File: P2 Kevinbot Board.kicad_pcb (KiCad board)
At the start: 2 copper layers, 196.5 x 95.4 mm, 56 parts, among them J11 Screw_Terminal_01x02, J13 Screw_Terminal_01x02, J14 Screw_Terminal_01x02, J17 Conn_01x02, J2 Conn_02x06_Odd_Even, J20 Conn_02x06_Odd_Even, J23 Conn_02x06_Odd_Even, J24 Conn_01x04, J25 Conn_01x04, J26 Conn_01x04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

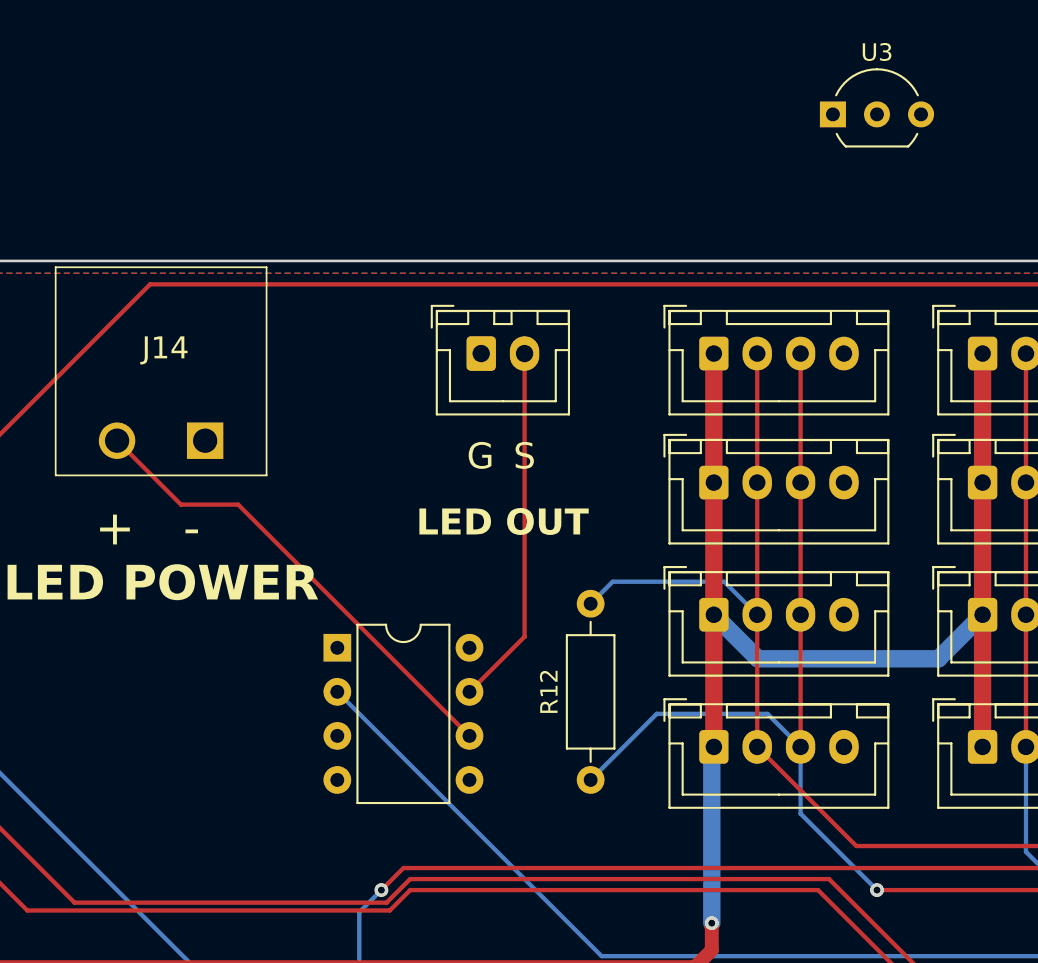
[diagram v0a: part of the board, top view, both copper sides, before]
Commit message: Add DS18B20
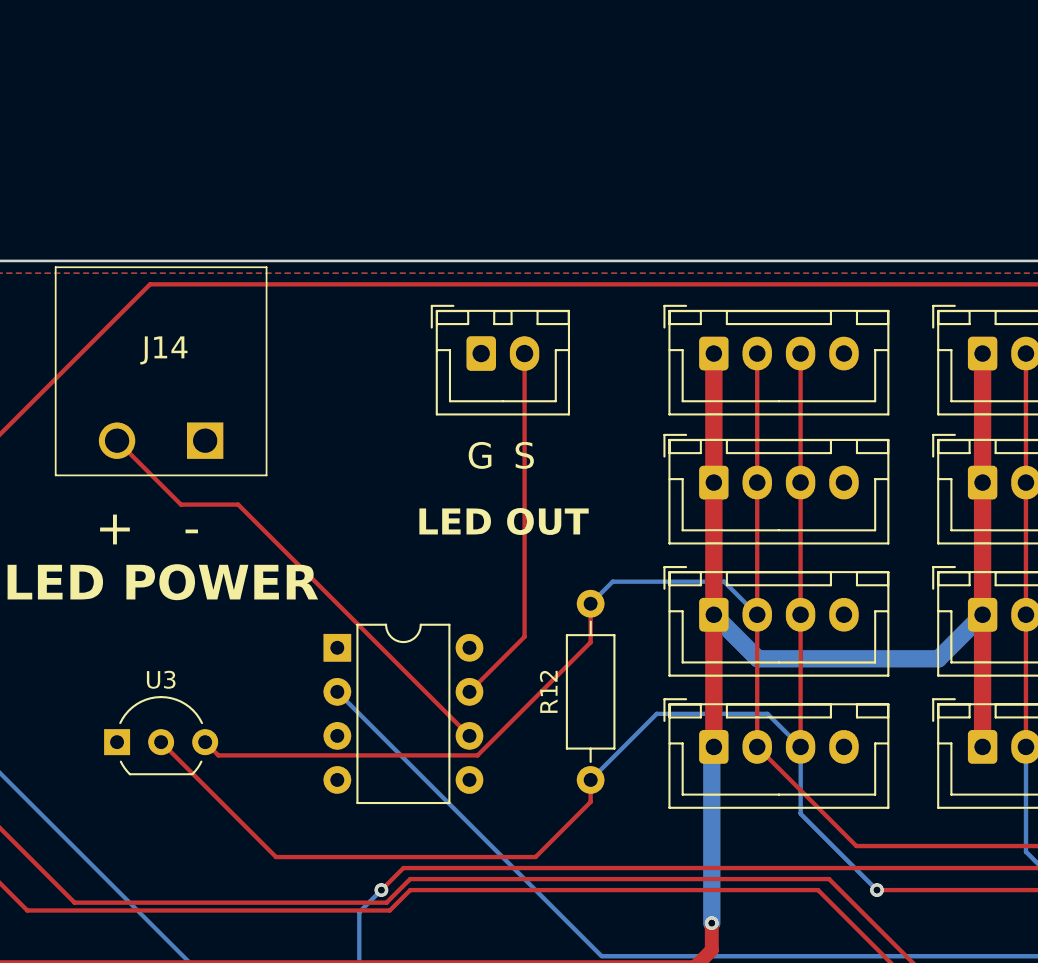
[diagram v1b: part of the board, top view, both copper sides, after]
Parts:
- moved U3 54.9 mm to (103.6, 82.9)
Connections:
- U3 pad 3: P2_V24 -> P2_V32
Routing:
- net P2_P39: track 91.2 -> 121.2 mm
- net P2_V32: track 97.4 -> 124.9 mm
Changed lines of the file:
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@@
   )
   (footprint "Package_TO_SOT_THT:TO-92_Inline_Wide" (layer "F.Cu")
-    (at 144.919 46.72)
+    (at 103.644 82.915)
     (descr "TO-92 leads in-line, wide, drill 0.75mm (see NXP sot054_po.pdf)")
     (tags "to-92 sc-43 sc-43a sot54 PA33 transistor")
@@
       (net 44 "P2_P39") (pinfunction "DQ") (pintype "bidirectional"))
     (pad "3" thru_hole circle (at 5.08 0) (size 1.5 1.5) (drill 0.8) (layers "*.Cu" "*.Mask")
-      (net 66 "P2_V24") (pinfunction "VDD") (pintype "power_in"))
+      (net 43 "P2_V32") (pinfunction "VDD") (pintype "power_in"))
     (model "${KICAD6_3DMODEL_DIR}/Package_TO_SOT_THT.3dshapes/TO-92_Inline_Wide.wrl"
       (offset (xyz 0 0 0))
@@
   (segment (start 189.789 100.216726) (end 189.305726 100.7) (width 0.25) (layer "F.Cu") (net 43))
   (segment (start 182.160726 88.905) (end 189.789 96.533274) (width 0.25) (layer "F.Cu") (net 43))
+  (segment (start 108.724 82.915) (end 109.489 83.68) (width 0.25) (layer "F.Cu") (net 43))
   (segment (start 146.269 88.905) (end 182.160726 88.905) (width 0.25) (layer "F.Cu") (net 43))
   (segment (start 140.554 83.19) (end 146.269 88.905) (width 0.25) (layer "F.Cu") (net 43))
   (segment (start 140.554 83.19) (end 140.554 60.51) (width 0.25) (layer "F.Cu") (net 43))
   (segment (start 189.305726 100.7) (end 187.352274 100.7) (width 0.25) (layer "F.Cu") (net 43))
+  (segment (start 109.489 83.68) (end 124.429991 83.68) (width 0.25) (layer "F.Cu") (net 43))
+  (segment (start 124.429991 83.68) (end 130.949 77.160991) (width 0.25) (layer "F.Cu") (net 43))
   (segment (start 187.352274 100.7) (end 186.424 99.771726) (width 0.25) (layer "F.Cu") (net 43))
+  (segment (start 130.949 77.160991) (end 130.949 74.935) (width 0.25) (layer "F.Cu") (net 43))
   (segment (start 186.424 99.771726) (end 186.424 98.375) (width 0.25) (layer "F.Cu") (net 43))
   (segment (start 189.789 96.533274) (end 189.789 100.216726) (width 0.25) (layer "F.Cu") (net 43))
@@
   (segment (start 187.694 98.375) (end 187.694 96.978274) (width 0.25) (layer "F.Cu") (net 44))
   (segment (start 182.160726 91.445) (end 147.459 91.445) (width 0.25) (layer "F.Cu") (net 44))
+  (segment (start 112.809 89.54) (end 127.774 89.54) (width 0.25) (layer "F.Cu") (net 44))
   (segment (start 143.054 60.51) (end 143.054 83.19) (width 0.25) (layer "F.Cu") (net 44))
+  (segment (start 130.949 86.365) (end 130.949 85.095) (width 0.25) (layer "F.Cu") (net 44))
+  (segment (start 106.184 82.915) (end 112.809 89.54) (width 0.25) (layer "F.Cu") (net 44))
+  (segment (start 127.774 89.54) (end 130.949 86.365) (width 0.25) (layer "F.Cu") (net 44))
   (via (at 147.459 91.445) (size 0.8) (drill 0.4) (layers "F.Cu" "B.Cu") (net 44))
   (segment (start 143.054 87.04) (end 143.054 83.19) (width 0.25) (layer "B.Cu") (net 44))

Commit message: Begin PCA placement
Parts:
- R5: footprint Resistor_THT:R_Axial_DIN0207_L6.3mm_D2.5mm_P10.16mm_Horizontal -> Resistor_THT:R_Axial_DIN0309_L9.0mm_D3.2mm_P2.54mm_Vertical
- moved R13 210.5 mm to (244.0, 106.5), turned to 90 degrees
- moved R19 196.4 mm to (229.4, 127.6), turned to 180 degrees
- moved R18 195.8 mm to (229.4, 121.3), turned to 180 degrees
- moved R17 195.3 mm to (229.4, 114.9), turned to 180 degrees
- moved R16 194.8 mm to (229.4, 108.6), turned to 180 degrees
- moved R15 194.4 mm to (229.4, 102.2), turned to 180 degrees
- moved R14 194.1 mm to (229.4, 95.9), turned to 180 degrees
- moved U4 192.8 mm to (238.0, 108.3)
- moved JP6 191.2 mm to (229.4, 124.5)
- moved JP5 190.7 mm to (229.4, 118.1)
- moved JP4 190.2 mm to (229.4, 111.8)
- moved JP3 189.8 mm to (229.4, 105.4)
- moved JP2 189.4 mm to (229.4, 99.1)
- moved JP1 189.1 mm to (229.4, 92.7)
- moved R5 184.4 mm to (241.0, 66.0), turned to 180 degrees
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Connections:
- J35 pad 2: P2_V16 -> P2_V40
- J36 pad 2: P2_V16 -> P2_V40
- J37 pad 2: P2_V16 -> P2_V40
- J38 pad 2: P2_V16 -> P2_V40
- JP1 pad 1: P2_V16 -> P2_V40
- JP2 pad 1: P2_V16 -> P2_V40
- JP3 pad 1: P2_V16 -> P2_V40
- JP4 pad 1: P2_V16 -> P2_V40
- JP5 pad 1: P2_V16 -> P2_V40
- JP6 pad 1: P2_V16 -> P2_V40
- U4 pad 28: P2_V16 -> P2_V40
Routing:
- net P2_V40: track 0.00 -> 189.5 mm, vias 0 -> 1
- net +5V: track 350.3 -> 434.8 mm
- net P2_V16: track 101.1 -> 61.2 mm, vias 2 -> 1
- net PCA_A4: track 0.00 -> 17.5 mm
- net PCA_A0: track 0.00 -> 13.4 mm
- net PCA_A3: track 0.00 -> 13.1 mm
- net PCA_A1: track 0.00 -> 8.77 mm
- net PCA_A2: track 0.00 -> 8.59 mm
- net Net-(D1-A): track 0.00 -> 5.24 mm
- net PCA_A5: track 0.00 -> 3.52 mm
- net Net-(U4-~{OE}): track 0.00 -> 3.44 mm
- net P2_P35: track 56.7 -> 57.6 mm
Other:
- board text added: "POWER"
- board text removed: "PWR"

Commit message: PCA routing
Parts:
- moved J31 237.1 mm to (258.6, 89.5), turned to -90 degrees
- moved J34 236.2 mm to (258.6, 125.7), turned to -90 degrees
- moved J33 236.0 mm to (258.6, 113.7), turned to -90 degrees
- moved J32 235.8 mm to (258.6, 101.6), turned to -90 degrees
- moved R13 2.55 mm to (246.5, 106.2)
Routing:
- net P2_P42: track 51.0 -> 131.8 mm, vias 1 -> 2
- net P2_P41: track 55.1 -> 131.6 mm, vias 1 -> 3
- net SVO_PWR: track 0.00 -> 52.4 mm
- net SVO14: track 0.00 -> 47.5 mm, vias 0 -> 1
- net SVO15: track 0.00 -> 39.8 mm, vias 0 -> 2
- net SVO4: track 0.00 -> 38.7 mm
- net SVO13: track 0.00 -> 37.3 mm, vias 0 -> 1
- net +5V: track 434.8 -> 466.6 mm
- net SVO3: track 0.00 -> 27.5 mm, vias 0 -> 2
- net SVO0: track 0.00 -> 26.2 mm, vias 0 -> 1
- net PCA_A5: track 3.52 -> 29.2 mm, vias 0 -> 2
- net SVO1: track 0.00 -> 25.0 mm, vias 0 -> 1
- net SVO12: track 0.00 -> 24.6 mm, vias 0 -> 1
- net SVO2: track 0.00 -> 24.2 mm, vias 0 -> 1
- net SVO11: track 0.00 -> 21.5 mm, vias 0 -> 1
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
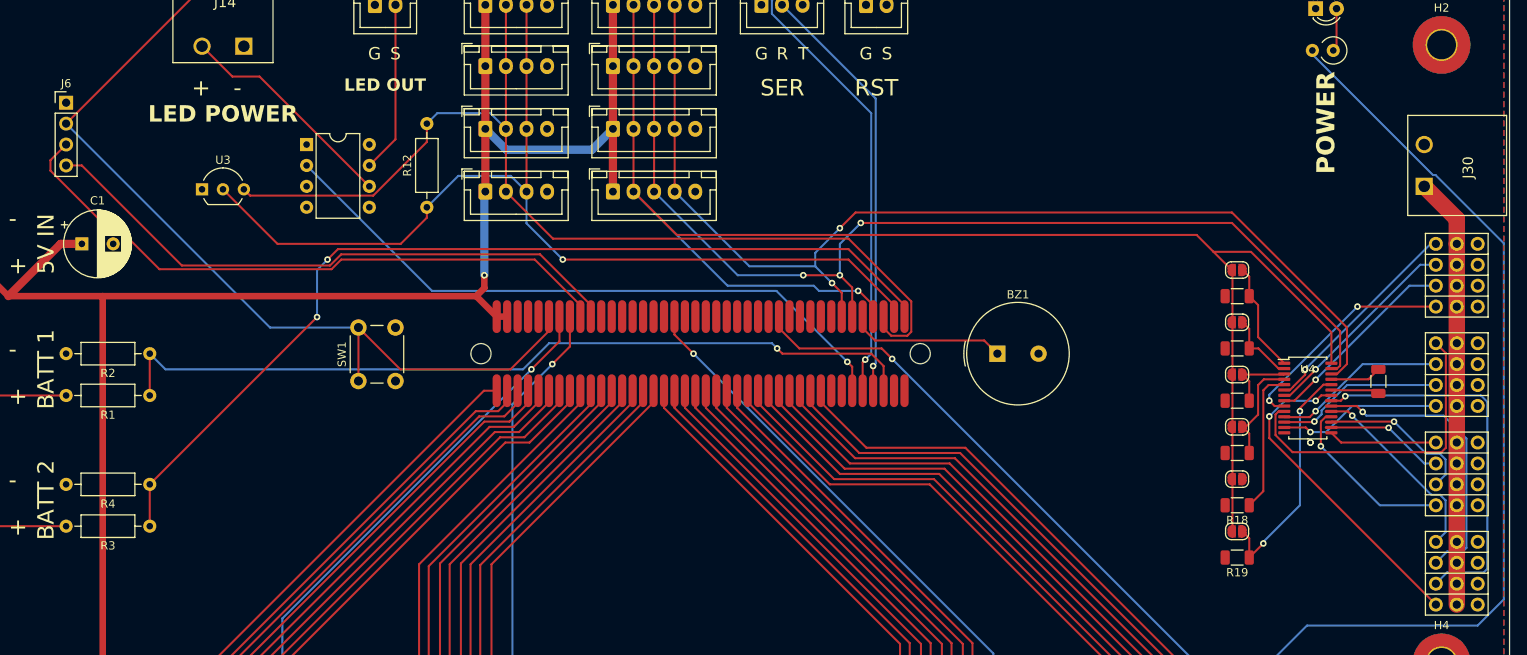
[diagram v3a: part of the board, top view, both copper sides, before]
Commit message: Finish PCA routing
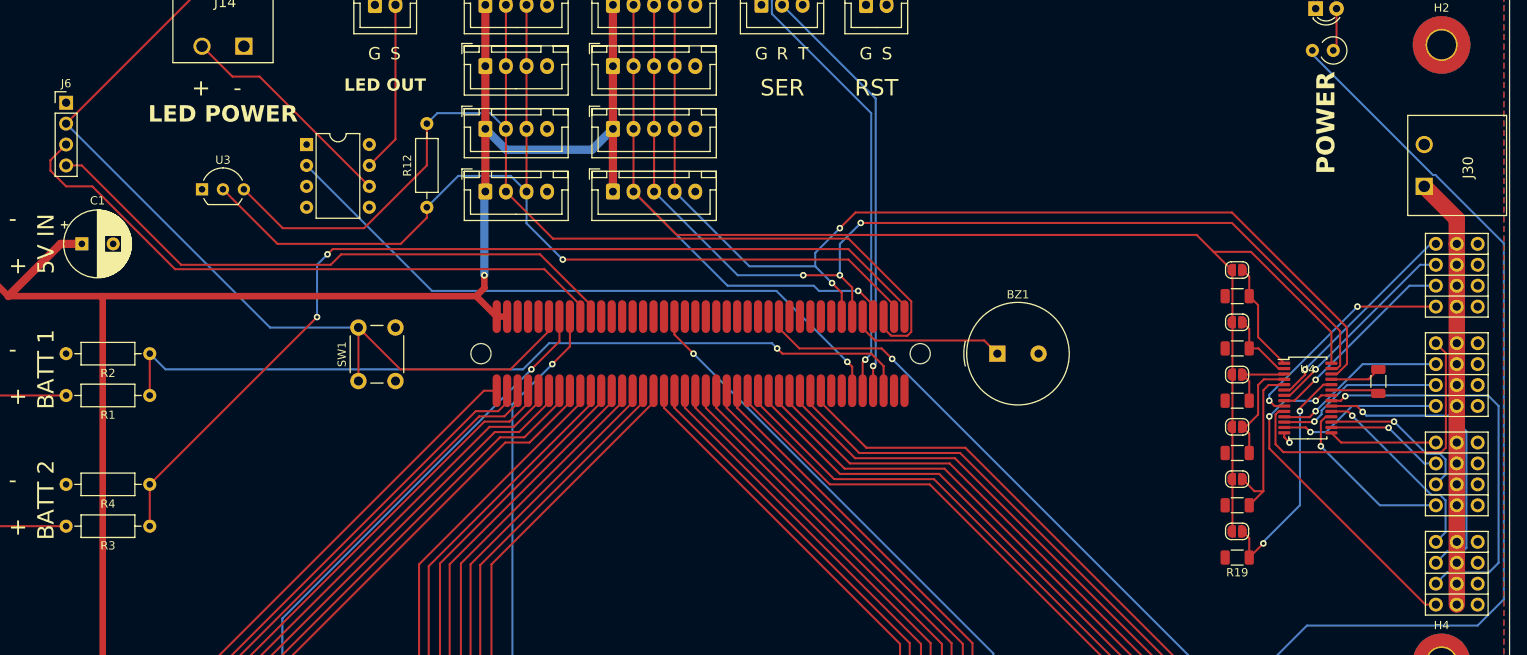
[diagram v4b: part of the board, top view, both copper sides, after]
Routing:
- net P2_V32: track 124.9 -> 129.8 mm
- net PCA_A4: track 17.5 -> 20.6 mm
- net -BATT: track 6.21 -> 7.65 mm, vias 2 -> 1
- net SVO14: track 47.5 -> 48.8 mm
- net P2_P63_RXD: track 77.5 -> 76.5 mm
- net SVO13: track 37.3 -> 36.3 mm
- net SVO15: track 39.8 -> 40.6 mm
- net SVO9: track 15.2 -> 14.5 mm
- net SVO12: track 24.6 -> 23.9 mm
- net SVO10: track 20.0 -> 19.3 mm
- net SVO4: track 38.7 -> 39.4 mm

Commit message: Cleanup
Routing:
- net +5V: track 466.2 -> 468.5 mm
- net PCA_A4: track 20.6 -> 20.0 mm
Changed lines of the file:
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@@
   (segment (start 113.399 146.055) (end 115.939 148.595) (width 0.8) (layer "F.Cu") (net 11))
   (segment (start 115.939 148.595) (end 138.799 148.595) (width 0.8) (layer "F.Cu") (net 11))
+  (segment (start 78.8485 89.54) (end 76.3085 92.08) (width 1) (layer "F.Cu") (net 11))
+  (segment (start 89.049 89.54) (end 78.8485 89.54) (width 1) (layer "F.Cu") (net 11))
   (segment (start 197.219 148.595) (end 199.759 146.055) (width 0.8) (layer "F.Cu") (net 11))
   (segment (start 115.939 148.595) (end 100.139 148.595) (width 0.8) (layer "F.Cu") (net 11))
   (segment (start 137.934 93.35) (end 137.934 94.905) (width 0.8) (layer "F.Cu") (net 11))
-  (segment (start 86.4685 89.54) (end 80.1185 95.89) (width 1) (layer "F.Cu") (net 11))
   (segment (start 91.579 140.035) (end 91.579 95.89) (width 0.8) (layer "F.Cu") (net 11))
-  (segment (start 89.049 89.54) (end 86.4685 89.54) (width 1) (layer "F.Cu") (net 11))
   (via (at 137.934 93.35) (size 0.8) (drill 0.4) (layers "F.Cu" "B.Cu") (net 11))
   (segment (start 140.594 78.11) (end 138.054 75.57) (width 1) (layer "B.Cu") (net 11))
@@
   (segment (start 231.914 106.685) (end 232.609 105.99) (width 0.25) (layer "F.Cu") (net 73))
   (segment (start 231.914 110.26962) (end 231.914 106.685) (width 0.25) (layer "F.Cu") (net 73))
-  (segment (start 230.009 118.115) (end 231.4715 119.5775) (width 0.25) (layer "F.Cu") (net 74))
+  (segment (start 230.009 118.115) (end 232.549 118.115) (width 0.25) (layer "F.Cu") (net 74))
+  (segment (start 232.549 118.115) (end 232.549 107.32) (width 0.25) (layer "F.Cu") (net 74))
   (segment (start 230.8365 121.29) (end 232.549 119.5775) (width 0.25) (layer "F.Cu") (net 74))
   (segment (start 233.184 106.685) (end 235.044 106.685) (width 0.25) (layer "F.Cu") (net 74))
+  (segment (start 232.549 119.5775) (end 232.549 118.115) (width 0.25) (layer "F.Cu") (net 74))
   (segment (start 232.549 107.32) (end 233.184 106.685) (width 0.25) (layer "F.Cu") (net 74))
-  (segment (start 232.549 119.5775) (end 232.549 107.32) (width 0.25) (layer "F.Cu") (net 74))
-  (segment (start 231.4715 119.5775) (end 232.549 119.5775) (width 0.25) (layer "F.Cu") (net 74))
   (segment (start 235.044 106.685) (end 235.089 106.64) (width 0.25) (layer "F.Cu") (net 74))
   (segment (start 236.994 109.498229) (end 239.852229 106.64) (width 0.25) (layer "F.Cu") (net 75))
@@
   (segment (start 259.854 107.955) (end 242.594 107.955) (width 0.25) (layer "B.Cu") (net 88))
   (segment (start 239.576828 107.94) (end 240.814 107.94) (width 0.25) (layer "F.Cu") (net 89))
-  (segment (start 252.234 133.355) (end 233.2735 114.3945) (width 0.25) (layer "F.Cu") (net 89))
-  (segment (start 233.2735 114.3945) (end 233.2735 110.495) (width 0.25) (layer "F.Cu") (net 89))
-  (segment (start 253.504 133.355) (end 252.234 133.355) (width 0.25) (layer "F.Cu") (net 89))
+  (segment (start 233.2735 113.760896) (end 233.2735 110.495) (width 0.25) (layer "F.Cu") (net 89))
   (segment (start 238.912914 108.603914) (end 239.576828 107.94) (width 0.25) (layer "F.Cu") (net 89))
+  (segment (start 252.867604 133.355) (end 233.2735 113.760896) (width 0.25) (layer "F.Cu") (net 89))
+  (segment (start 253.504 133.355) (end 252.867604 133.355) (width 0.25) (layer "F.Cu") (net 89))
   (via (at 233.2735 110.495) (size 0.8) (drill 0.4) (layers "F.Cu" "B.Cu") (net 89))
   (via (at 238.912914 108.603914) (size 0.8) (drill 0.4) (layers "F.Cu" "B.Cu") (net 89))

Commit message: Board cleanup
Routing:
- net P2_P62_TXD: track 73.2 -> 72.2 mm
- net P2_P39: track 121.2 -> 120.7 mm
